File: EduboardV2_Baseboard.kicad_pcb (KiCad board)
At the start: 2 copper layers, 100 x 160 mm, 167 parts, among them IC201 PCF8563T_5,518, IC202 W25Q128JVSIQTR, IC301 XL1509-5.0E1, IC302 SY8113BADC, IC501 USB2514BI-AEZG-TR, IC601 SP3485EN-L_TR, IC602 WM8782SEDS_RV_C323842, IC603 STK8321, IC604 CS4344-CZZ, IC605 STK8321, IC606 MCP9700AT-E_TT, J501 Conn_WS2812_Extern, Q301 AO3401A, Q302 AO3400A, Q303 AO3401A, Q304 AO3401A, SW301 1FS1T1B9M2RES-5, SW401 K2-1102SP-C4SC-04, SW402 K2-1102SP-C4SC-04, SW403 K2-1102SP-C4SC-04, SW404 K2-1102SP-C4SC-04, SW405 PEC11R-4220F-S0012, T401 AO3400A, T402 AO3400A, T403 AO3400A, T404 AO3400A, T405 AO3400A, T406 AO3400A, T501 AO3400A, T502 AO3400A, X201 PCIE-52P40H, X202 32.768 kHz, X203 TF-15×15, X204 CR1220-2ZX, X301 KF2EDGR-3.81-3P, X401 ER-TFT035-6, X501 BH-00105, X502 USB3.1C16PFSMT, X503 USB3.1C16PFSMT, X504 S4B-PH-SM4-K-TB(LF)(SN), X505 PJ-327C-4A, X506 PJ-327C-4A, X507 KF2EDGR-3.81-3P, X601 CH340G, Y601 X322512MSB4SI

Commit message: start rework of baseboard.
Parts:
- removed BUZZER401: MLT-8530, eduboardv2:BUZ-SMD_4P-L8.5-W8.5-P8.50-TL
- removed C201: 10pF, eduboardv2:C0402
- removed C202, C410, C411: 1uF, eduboardv2:C0402
- removed C203, C402, C404, C406, C408: 10nF, eduboardv2:C0402
- removed C204, C407, C409, C604, C606, C608: 100nF, eduboardv2:C0402
- removed C301, C305, C312: 220uF, 35V, eduboardv2:CAP-SMD_BD8.0-L8.3-W8.3-RD
- removed C302, C307, C310, C601, C605: 100nF, 50V, eduboardv2:C0402
- removed C303, C306, C309: 10uF, X5R, 25V, eduboardv2:C0603
- removed C304, C602, C603: 22pF, eduboardv2:C0402
- removed C308, C311: 1uF, 25V, eduboardv2:C0402
- removed C401, C403, C405: 1nF, eduboardv2:C0402
- removed C607, C609: 10uF, eduboardv2:C0603
- removed C610, C611: 4.7uF, eduboardv2:C0603
- removed C612, C613: 2.2nF, eduboardv2:C0402
- removed D201, D202: B5819W_C8598, eduboardv2:SOD-123_L2.7-W1.6-LS3.7-RD-1
- removed D301, D302: SS210, eduboardv2:SMA_L4.3-W2.6-LS5.2-RD
- removed D303, D401, D402, D403, D404, D405, D406, D407, D408: blue, eduboardv2:LED0603-R-RD_BLUE
- removed D409: RGB-LED, eduboardv2:LED-SMD_FM-B2020RGBA-HG
- removed D410: WS2812B-B_W, eduboardv2:LED-SMD_4P-L5.0-W5.0-TL_WS2812B-B
- removed D411: 1N4148WST4, eduboardv2:SOD-323_L1.8-W1.3-LS2.5-RD
- removed D501, D502: PRTR5V0U2X_C2827688, eduboardv2:SOT-143-4_L2.9-W1.3-P1.92-LS2.4-BL
- removed IC201: PCF8563T_5,518, eduboardv2:SOIC-8_L5.0-W4.0-P1.27-LS6.0-BL
- removed IC202: W25Q128JVSIQTR, eduboardv2:SOIC-8_L5.3-W5.3-P1.27-LS8.0-BL
- removed IC301: XL1509-5.0E1, eduboardv2:SOIC-8_L5.0-W4.0-P1.27-LS6.0-BL
- removed IC302: SY8113BADC, eduboardv2:TSOT-23-6_L2.9-W1.6-P0.95-LS2.8-BR
- removed IC501: USB2514BI-AEZG-TR, eduboardv2:QFN-36_L6.0-W6.0-P0.50-BL-EP
- removed IC601: SP3485EN-L_TR, eduboardv2:SOIC-8_L5.0-W4.0-P1.27-LS6.0-BL
- removed IC602: WM8782SEDS_RV_C323842, eduboardv2:SSOP-20_L7.5-W5.2-P0.65-LS8.0-BL
- removed IC603, IC605: STK8321, eduboardv2:LGA-12_L2.0-W2.0-P0.50-TR
- removed IC604: CS4344-CZZ, eduboardv2:TSSOP-10_L3.0-W3.0-P0.50-LS4.9-BL
- removed IC606: MCP9700AT-E_TT, eduboardv2:SOT-23-3_L2.9-W1.3-P1.90-LS2.4-BR
- removed J501: Conn_WS2812_Extern, Connector_PinHeader_2.54mm:PinHeader_1x03_P2.54mm_Vertical
- removed JP501: Stemma Voltage Selector, Jumper:SolderJumper-3_P1.3mm_Open_RoundedPad1.0x1.5mm
- removed L301: 6.8uH, 1A, eduboardv2:IND-SMD_L4.0-W4.0
- removed L302: 68uH, 1A, eduboardv2:IND-SMD_L6.0-W6.0_FNR60XXS
- removed L601: GZ1608D601TF, eduboardv2:L0603
- removed Q301, Q303, Q304: AO3401A, eduboardv2:SOT-23_L2.9-W1.3-P1.90-LS2.4-BR
- removed Q302, T401, T402, T403, T404, T405, T406, T501, T502: AO3400A, eduboardv2:SOT-23-3_L2.9-W1.6-P1.90-LS2.8-BR
- removed R201, R202, R402, R409, R417, R421, R426, R427, R428, R429, R503, R504, R601, R603, R604, R605: 10k, eduboardv2:R0402
- removed R301, R302, R303: 1M, eduboardv2:R0402
- removed R304, R306: 100k, eduboardv2:R0402
- removed R305: 22k, eduboardv2:R0402
- removed R307, R401, R403, R405, R406, R407, R408, R410, R412, R413, R414, R416, R420: 1k, eduboardv2:R0402
- removed R404, R411, R415: 50k, eduboardv2:RES-TH_RK09K1130AAU
- removed R418, R419, R422: 150R, eduboardv2:R0402
- removed R423, R424, R425, R430, R431, R432, R434, R436, R437, R439: 10R, eduboardv2:R0402
- removed R433, R435, R438: NP, eduboardv2:R0402
- removed R501, R502: 5.1k, eduboardv2:R0402
- removed R602: 120R, eduboardv2:R0402
- removed R606, R607: 470R, eduboardv2:R0402
- removed SW301: 1FS1T1B9M2RES-5, eduboardv2:SW-TH_1FS1T1B9M2RES-5
- removed SW401, SW402, SW403, SW404: K2-1102SP-C4SC-04, eduboardv2:KEY-SMD_4P-L6.0-W6.0-P4.50-LS9.5-BL
- removed SW405: PEC11R-4220F-S0012, eduboardv2:SW-TH_PEC11R-4220F-S0012
- removed X201: PCIE-52P40H, eduboardv2:PCIE-SMD_PCIE-52P40H
- removed X202: 32.768 kHz, eduboardv2:FC-135R_L3.2-W1.5
- removed X203: TF-15×15, eduboardv2:TF-SMD_TF-15-15
- removed X204: CR1220-2ZX, eduboardv2:BAT-SMD_CR1220-2ZX
- removed X301, X507: KF2EDGR-3.81-3P, eduboardv2:CONN-TH_3P-P3.81_KF2EDGR-3.81-3P
- removed X401: ER-TFT035-6, eduboardv2:FPC-SMD_AFC07-S50ECA-00
- removed X501: BH-00105, eduboardv2:IDC-SMD_BH-00105
- removed X502, X503: USB3.1C16PFSMT, eduboardv2:USB-C-SMD_TYPE-C-USB-17
- removed X504: S4B-PH-SM4-K-TB(LF)(SN), eduboardv2:CONN-SMD_S4B-PH-SM4-K-TB-LF-SN
- removed X505, X506: PJ-327C-4A, eduboardv2:AUDIO-SMD_PJ-327C-4A
- removed X601: CH340G, eduboardv2:SOIC-16_L9.9-W3.9-P1.27-LS6.0-BL
- removed Y601: X322512MSB4SI, eduboardv2:OSC-SMD_4P-L3.2-W2.5-BL

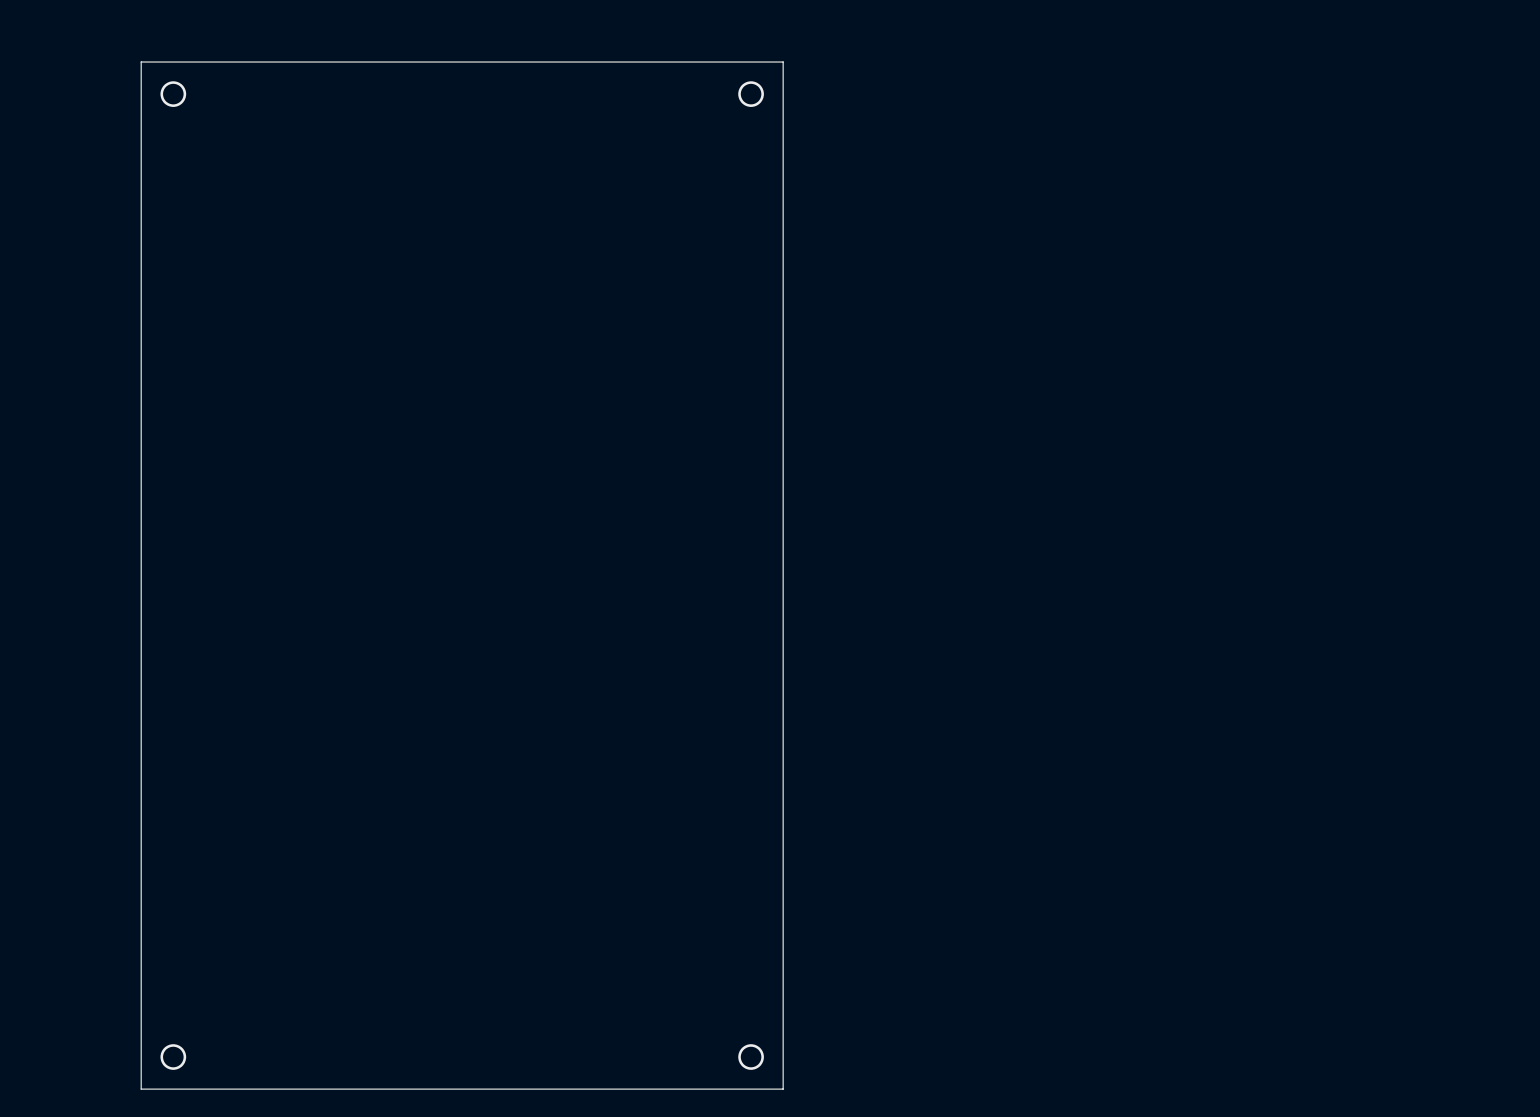
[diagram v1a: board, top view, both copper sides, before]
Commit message: replace display with better module, start layout parts on pcb.
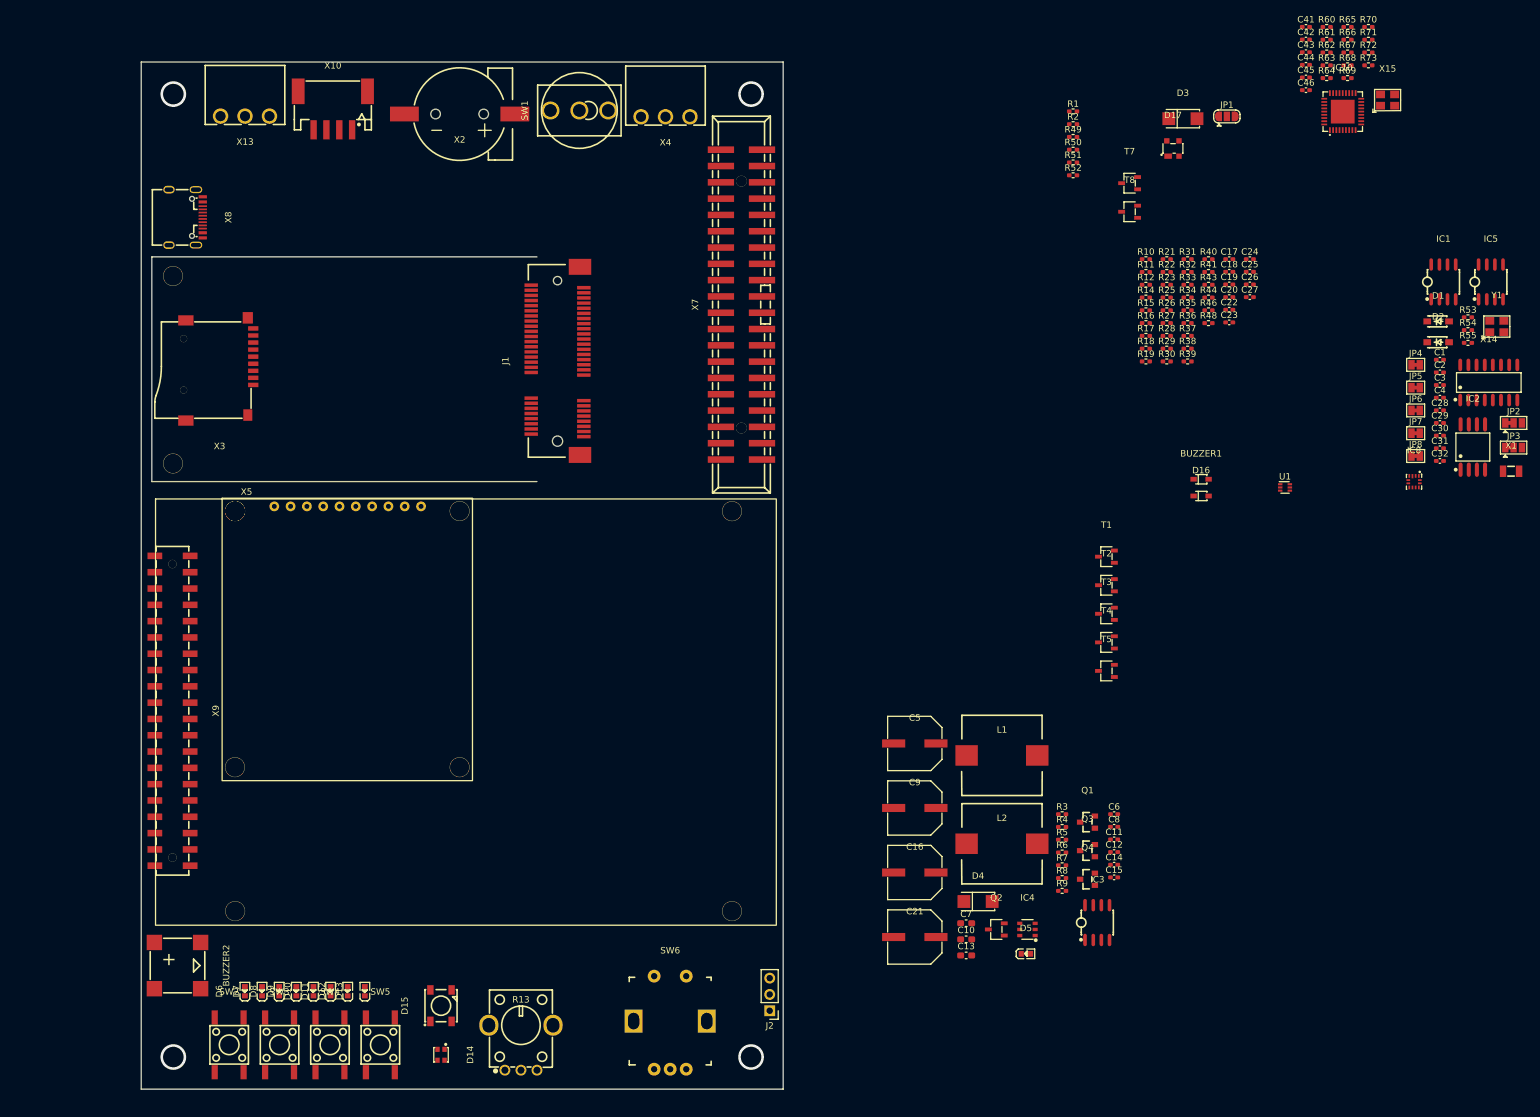
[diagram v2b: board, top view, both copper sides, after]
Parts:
- added BUZZER1: MLT-8530, EduboardV2_kicadlib:SOD-323_L1.8-W1.3-LS2.5-RD, F.Cu at (219.1, 86.0)
- added BUZZER2: MLT-8530, EduboardV2_kicadlib:BUZ-SMD_4P-L8.5-W8.5-P8.50-BR, F.Cu at (59.6, 161.8)
- added C1: 10pF, Capacitor_SMD:C_0402_1005Metric_Pad0.74x0.62mm_HandSolder, F.Cu at (256.3, 67.4)
- added C10: 10uF, X5R, 25V, Capacitor_SMD:C_0603_1608Metric_Pad1.08x0.95mm_HandSolder, F.Cu at (182.5, 157.7)
- added C11: 100nF, 50V, Capacitor_SMD:C_0402_1005Metric_Pad0.74x0.62mm_HandSolder, F.Cu at (205.6, 142.1)
- added C12: 1uF, 25V, Capacitor_SMD:C_0402_1005Metric_Pad0.74x0.62mm_HandSolder, F.Cu at (205.6, 144.1)
- added C13: 10uF, X5R, 25V, Capacitor_SMD:C_0603_1608Metric_Pad1.08x0.95mm_HandSolder, F.Cu at (182.5, 160.2)
- added C14: 100nF, 50V, Capacitor_SMD:C_0402_1005Metric_Pad0.74x0.62mm_HandSolder, F.Cu at (205.6, 146.0)
- added C15: 1uF, 25V, Capacitor_SMD:C_0402_1005Metric_Pad0.74x0.62mm_HandSolder, F.Cu at (205.6, 148.0)
- added C16: 220uF, 35V, EduboardV2_kicadlib:CAP-SMD_BD8.0-L8.3-W8.3-RD, F.Cu at (174.5, 147.3)
- added C17: 1nF, Capacitor_SMD:C_0402_1005Metric_Pad0.74x0.62mm_HandSolder, F.Cu at (223.5, 51.7)
- added C18: 10nF, Capacitor_SMD:C_0402_1005Metric_Pad0.74x0.62mm_HandSolder, F.Cu at (223.5, 53.7)
- added C19: 100nF, Capacitor_SMD:C_0402_1005Metric_Pad0.74x0.62mm_HandSolder, F.Cu at (223.5, 55.7)
- added C2: 1uF, Capacitor_SMD:C_0402_1005Metric_Pad0.74x0.62mm_HandSolder, F.Cu at (256.3, 69.4)
- added C20: 10nF, Capacitor_SMD:C_0402_1005Metric_Pad0.74x0.62mm_HandSolder, F.Cu at (223.5, 57.6)
- added C21: 220uF, 35V, EduboardV2_kicadlib:CAP-SMD_BD8.0-L8.3-W8.3-RD, F.Cu at (174.5, 157.3)
- added C22: 10nF, Capacitor_SMD:C_0402_1005Metric_Pad0.74x0.62mm_HandSolder, F.Cu at (223.5, 59.6)
- added C23: 100nF, Capacitor_SMD:C_0402_1005Metric_Pad0.74x0.62mm_HandSolder, F.Cu at (223.5, 61.6)
- added C24: 10nF, Capacitor_SMD:C_0402_1005Metric_Pad0.74x0.62mm_HandSolder, F.Cu at (226.7, 51.7)
- added C25: 100nF, Capacitor_SMD:C_0402_1005Metric_Pad0.74x0.62mm_HandSolder, F.Cu at (226.7, 53.7)
- added C26: 1uF, Capacitor_SMD:C_0402_1005Metric_Pad0.74x0.62mm_HandSolder, F.Cu at (226.7, 55.7)
- added C27: 1uF, Capacitor_SMD:C_0402_1005Metric_Pad0.74x0.62mm_HandSolder, F.Cu at (226.7, 57.6)
- added C28: 100nF, 50V, Capacitor_SMD:C_0402_1005Metric_Pad0.74x0.62mm_HandSolder, F.Cu at (256.3, 75.3)
- added C29: 22pF, Capacitor_SMD:C_0402_1005Metric_Pad0.74x0.62mm_HandSolder, F.Cu at (256.3, 77.2)
- added C3: 10nF, Capacitor_SMD:C_0402_1005Metric_Pad0.74x0.62mm_HandSolder, F.Cu at (256.3, 71.3)
- added C30: 22pF, Capacitor_SMD:C_0402_1005Metric_Pad0.74x0.62mm_HandSolder, F.Cu at (256.3, 79.2)
- added C31: 100nF, Capacitor_SMD:C_0402_1005Metric_Pad0.74x0.62mm_HandSolder, F.Cu at (256.3, 81.2)
- added C32: 100nF, 50V, Capacitor_SMD:C_0402_1005Metric_Pad0.74x0.62mm_HandSolder, F.Cu at (256.3, 83.1)
- added C4: 100nF, Capacitor_SMD:C_0402_1005Metric_Pad0.74x0.62mm_HandSolder, F.Cu at (256.3, 73.3)
- added C41: 100nF, 50V, Capacitor_SMD:C_0402_1005Metric_Pad0.74x0.62mm_HandSolder, F.Cu at (235.4, 15.5)
- added C42: CL05C100JB5NNNC, Capacitor_SMD:C_0402_1005Metric_Pad0.74x0.62mm_HandSolder, F.Cu at (235.4, 17.5)
- added C43: 100nF, 50V, Capacitor_SMD:C_0402_1005Metric_Pad0.74x0.62mm_HandSolder, F.Cu at (235.4, 19.5)
- added C44: CL05C100JB5NNNC, Capacitor_SMD:C_0402_1005Metric_Pad0.74x0.62mm_HandSolder, F.Cu at (235.4, 21.4)
- added C45: 100nF, 50V, Capacitor_SMD:C_0402_1005Metric_Pad0.74x0.62mm_HandSolder, F.Cu at (235.4, 23.4)
- added C46: 100nF, 50V, Capacitor_SMD:C_0402_1005Metric_Pad0.74x0.62mm_HandSolder, F.Cu at (235.4, 25.4)
- added C5: 220uF, 35V, EduboardV2_kicadlib:CAP-SMD_BD8.0-L8.3-W8.3-RD, F.Cu at (174.5, 127.2)
- added C6: 100nF, 50V, Capacitor_SMD:C_0402_1005Metric_Pad0.74x0.62mm_HandSolder, F.Cu at (205.6, 138.2)
- added C7: 10uF, X5R, 25V, Capacitor_SMD:C_0603_1608Metric_Pad1.08x0.95mm_HandSolder, F.Cu at (182.5, 155.2)
- added C8: 22pF, Capacitor_SMD:C_0402_1005Metric_Pad0.74x0.62mm_HandSolder, F.Cu at (205.6, 140.1)
- added C9: 220uF, 35V, EduboardV2_kicadlib:CAP-SMD_BD8.0-L8.3-W8.3-RD, F.Cu at (174.5, 137.2)
- added D1: B5819W_C8598, EduboardV2_kicadlib:SOD-123_L2.7-W1.6-LS3.7-RD-1, F.Cu at (256.0, 61.4)
- added D10: blue, EduboardV2_kicadlib:LED0603-FD_BLUE, F.Cu at (80.8, 165.8)
- added D11: blue, EduboardV2_kicadlib:LED0603-FD_BLUE, F.Cu at (83.5, 165.8)
- added D12: blue, EduboardV2_kicadlib:LED0603-FD_BLUE, F.Cu at (86.2, 165.8)
- added D13: blue, EduboardV2_kicadlib:LED0603-FD_BLUE, F.Cu at (88.8, 165.8)
- added D14: RGB-LED, EduboardV2_kicadlib:LED-SMD_FM-B2020RGBA-HG, F.Cu at (100.7, 175.7)
- added D15: WS2812B-B_W, EduboardV2_kicadlib:LED-SMD_4P-L5.0-W5.0-TL_WS2812B-B, F.Cu at (100.7, 168.0)
- added D16: 1N4148WST4, EduboardV2_kicadlib:SOD-323_L1.8-W1.3-LS2.5-RD, F.Cu at (219.1, 88.6)
- added D17: PRTR5V0U2X_C2827688, EduboardV2_kicadlib:SOT-143-4_L2.9-W1.3-P1.92-LS2.4-BL, F.Cu at (214.7, 34.5)
- added D2: B5819W_C8598, EduboardV2_kicadlib:SOD-123_L2.7-W1.6-LS3.7-RD-1, F.Cu at (256.0, 64.7)
- added D3: SS210, EduboardV2_kicadlib:SMA_L4.3-W2.6-LS5.2-RD, F.Cu at (216.3, 29.8)
- added D4: SS210, EduboardV2_kicadlib:SMA_L4.3-W2.6-LS5.2-RD, F.Cu at (184.4, 151.8)
- added D5: blue, EduboardV2_kicadlib:LED0603-FD_BLUE, F.Cu at (191.8, 159.9)
- added D6: blue, EduboardV2_kicadlib:LED0603-FD_BLUE, F.Cu at (70.2, 165.8)
- added D7: blue, EduboardV2_kicadlib:LED0603-FD_BLUE, F.Cu at (72.8, 165.8)
- added D8: blue, EduboardV2_kicadlib:LED0603-FD_BLUE, F.Cu at (75.5, 165.8)
- added D9: blue, EduboardV2_kicadlib:LED0603-FD_BLUE, F.Cu at (78.2, 165.8)
- added IC1: PCF8563T_5,518, EduboardV2_kicadlib:SOIC-8_L5.0-W4.0-P1.27-LS6.0-BL, F.Cu at (256.9, 55.3)
- added IC10: USB2514BI-AEZG-TR, EduboardV2_kicadlib:TQFN-36_L6.0-W6.0-P0.50-BL-EP3.7, F.Cu at (241.2, 28.7)
- added IC2: W25Q128JVSIQTR, EduboardV2_kicadlib:SOIC-8_L5.3-W5.3-P1.27-LS8.0-BL, F.Cu at (261.4, 81.0)
- added IC3: XL1509-5.0E1, EduboardV2_kicadlib:SOIC-8_L5.0-W4.0-P1.27-LS6.0-BL, F.Cu at (202.9, 155.1)
- added IC4: SY8113BADC, EduboardV2_kicadlib:TSOT-23-6_L2.9-W1.6-P0.95-LS2.8-BR, F.Cu at (192.1, 156.1)
- added IC5: SP3485EN-L_TR, EduboardV2_kicadlib:SOIC-8_L5.0-W4.0-P1.27-LS6.0-BL, F.Cu at (264.2, 55.3)
- added IC8: STK8321, EduboardV2_kicadlib:LGA-12_L2.0-W2.0-P0.50-TR, F.Cu at (252.3, 86.4)
- added J1: EduboardV2 PCIE UP Board Connector, EduboardV2_kicadlib:CONN-SMD_52P-P0.80-V_91304-70-052RXXX, F.Cu at (118.8, 67.6)
- added J2: Conn_WS2812_Extern, Connector_PinHeader_2.54mm:PinHeader_1x03_P2.54mm_Vertical, F.Cu at (151.9, 168.8)
- added JP1: Stemma Voltage Selector, Jumper:SolderJumper-3_P1.3mm_Open_RoundedPad1.0x1.5mm, F.Cu at (223.1, 29.5)
- added JP2: SolderJumper_3_Bridged12, Jumper:SolderJumper-3_P1.3mm_Bridged12_Pad1.0x1.5mm, F.Cu at (267.8, 77.2)
- added JP3: SolderJumper_3_Bridged12, Jumper:SolderJumper-3_P1.3mm_Bridged12_Pad1.0x1.5mm, F.Cu at (267.8, 81.1)
- added JP4: SolderJumper_2_Bridged, Jumper:SolderJumper-2_P1.3mm_Bridged_Pad1.0x1.5mm, F.Cu at (252.5, 68.2)
- added JP5: SolderJumper_2_Bridged, Jumper:SolderJumper-2_P1.3mm_Bridged_Pad1.0x1.5mm, F.Cu at (252.5, 71.7)
- added JP6: SolderJumper_2_Bridged, Jumper:SolderJumper-2_P1.3mm_Bridged_Pad1.0x1.5mm, F.Cu at (252.5, 75.3)
- added JP7: SolderJumper_2_Bridged, Jumper:SolderJumper-2_P1.3mm_Bridged_Pad1.0x1.5mm, F.Cu at (252.5, 78.8)
- added JP8: SolderJumper_2_Bridged, Jumper:SolderJumper-2_P1.3mm_Bridged_Pad1.0x1.5mm, F.Cu at (252.5, 82.4)
- added L1: SLF12565T-680M2R0-PF, EduboardV2_kicadlib:IND-SMD_L12.5-W12.5_SLF12565T, F.Cu at (188.1, 129.0)
- added L2: SLF12565T-680M2R0-PF, EduboardV2_kicadlib:IND-SMD_L12.5-W12.5_SLF12565T, F.Cu at (188.1, 142.8)
- added Q1: AO3401A, EduboardV2_kicadlib:SOT-23_L2.9-W1.3-P1.90-LS2.4-BR, F.Cu at (201.4, 139.4)
- added Q2: AO3400A, EduboardV2_kicadlib:SOT-23-3_L2.9-W1.6-P1.90-LS2.8-BR, F.Cu at (187.2, 156.1)
- added Q3: AO3401A, EduboardV2_kicadlib:SOT-23_L2.9-W1.3-P1.90-LS2.4-BR, F.Cu at (201.4, 143.9)
- added Q4: AO3401A, EduboardV2_kicadlib:SOT-23_L2.9-W1.3-P1.90-LS2.4-BR, F.Cu at (201.4, 148.3)
- added R1: 10k, Resistor_SMD:R_0402_1005Metric_Pad0.72x0.64mm_HandSolder, F.Cu at (199.2, 28.7)
- added R10: 1k, Resistor_SMD:R_0402_1005Metric_Pad0.72x0.64mm_HandSolder, F.Cu at (210.5, 51.7)
- added R11: 10k, Resistor_SMD:R_0402_1005Metric_Pad0.72x0.64mm_HandSolder, F.Cu at (210.5, 53.7)
- added R12: 1k, Resistor_SMD:R_0402_1005Metric_Pad0.72x0.64mm_HandSolder, F.Cu at (210.5, 55.7)
- added R13: 50k, EduboardV2_kicadlib:RES-TH_RK09K1130AAU, F.Cu at (113.2, 174.6)
- added R14: 1k, Resistor_SMD:R_0402_1005Metric_Pad0.72x0.64mm_HandSolder, F.Cu at (210.5, 57.7)
- added R15: 1k, Resistor_SMD:R_0402_1005Metric_Pad0.72x0.64mm_HandSolder, F.Cu at (210.5, 59.7)
- added R16: 1k, Resistor_SMD:R_0402_1005Metric_Pad0.72x0.64mm_HandSolder, F.Cu at (210.5, 61.7)
- added R17: 1k, Resistor_SMD:R_0402_1005Metric_Pad0.72x0.64mm_HandSolder, F.Cu at (210.5, 63.7)
- added R18: 10k, Resistor_SMD:R_0402_1005Metric_Pad0.72x0.64mm_HandSolder, F.Cu at (210.5, 65.7)
- added R19: 1k, Resistor_SMD:R_0402_1005Metric_Pad0.72x0.64mm_HandSolder, F.Cu at (210.5, 67.6)
- added R2: 10k, Resistor_SMD:R_0402_1005Metric_Pad0.72x0.64mm_HandSolder, F.Cu at (199.2, 30.7)
- added R21: 1k, Resistor_SMD:R_0402_1005Metric_Pad0.72x0.64mm_HandSolder, F.Cu at (213.8, 51.7)
- added R22: 1k, Resistor_SMD:R_0402_1005Metric_Pad0.72x0.64mm_HandSolder, F.Cu at (213.8, 53.7)
- added R23: 1k, Resistor_SMD:R_0402_1005Metric_Pad0.72x0.64mm_HandSolder, F.Cu at (213.8, 55.7)
- added R25: 1k, Resistor_SMD:R_0402_1005Metric_Pad0.72x0.64mm_HandSolder, F.Cu at (213.8, 57.7)
- added R26: 10k, Resistor_SMD:R_0402_1005Metric_Pad0.72x0.64mm_HandSolder, F.Cu at (213.8, 59.7)
- added R27: 150R, Resistor_SMD:R_0402_1005Metric_Pad0.72x0.64mm_HandSolder, F.Cu at (213.8, 61.7)
- added R28: 150R, Resistor_SMD:R_0402_1005Metric_Pad0.72x0.64mm_HandSolder, F.Cu at (213.8, 63.7)
- added R29: 1k, Resistor_SMD:R_0402_1005Metric_Pad0.72x0.64mm_HandSolder, F.Cu at (213.8, 65.7)
- added R3: 1M, Resistor_SMD:R_0402_1005Metric_Pad0.72x0.64mm_HandSolder, F.Cu at (197.5, 138.2)
- added R30: 10k, Resistor_SMD:R_0402_1005Metric_Pad0.72x0.64mm_HandSolder, F.Cu at (213.8, 67.6)
- added R31: 150R, Resistor_SMD:R_0402_1005Metric_Pad0.72x0.64mm_HandSolder, F.Cu at (217.0, 51.7)
- added R32: 10R, Resistor_SMD:R_0402_1005Metric_Pad0.72x0.64mm_HandSolder, F.Cu at (217.0, 53.7)
- added R33: 10R, Resistor_SMD:R_0402_1005Metric_Pad0.72x0.64mm_HandSolder, F.Cu at (217.0, 55.7)
- added R34: 10R, Resistor_SMD:R_0402_1005Metric_Pad0.72x0.64mm_HandSolder, F.Cu at (217.0, 57.7)
- added R35: 10k, Resistor_SMD:R_0402_1005Metric_Pad0.72x0.64mm_HandSolder, F.Cu at (217.0, 59.7)
- added R36: 10k, Resistor_SMD:R_0402_1005Metric_Pad0.72x0.64mm_HandSolder, F.Cu at (217.0, 61.7)
- added R37: 10k, Resistor_SMD:R_0402_1005Metric_Pad0.72x0.64mm_HandSolder, F.Cu at (217.0, 63.7)
- added R38: 10k, Resistor_SMD:R_0402_1005Metric_Pad0.72x0.64mm_HandSolder, F.Cu at (217.0, 65.7)
- added R39: 10R, Resistor_SMD:R_0402_1005Metric_Pad0.72x0.64mm_HandSolder, F.Cu at (217.0, 67.6)
- added R4: 1M, Resistor_SMD:R_0402_1005Metric_Pad0.72x0.64mm_HandSolder, F.Cu at (197.5, 140.2)
- added R40: 10R, Resistor_SMD:R_0402_1005Metric_Pad0.72x0.64mm_HandSolder, F.Cu at (220.3, 51.7)
- added R41: 10R, Resistor_SMD:R_0402_1005Metric_Pad0.72x0.64mm_HandSolder, F.Cu at (220.3, 53.7)
- added R43: 10R, Resistor_SMD:R_0402_1005Metric_Pad0.72x0.64mm_HandSolder, F.Cu at (220.3, 55.7)
- added R44: NP, Resistor_SMD:R_0402_1005Metric_Pad0.72x0.64mm_HandSolder, F.Cu at (220.3, 57.7)
- added R46: 10R, Resistor_SMD:R_0402_1005Metric_Pad0.72x0.64mm_HandSolder, F.Cu at (220.3, 59.7)
- added R48: 10R, Resistor_SMD:R_0402_1005Metric_Pad0.72x0.64mm_HandSolder, F.Cu at (220.3, 61.7)
- added R49: 5.1k, Resistor_SMD:R_0402_1005Metric_Pad0.72x0.64mm_HandSolder, F.Cu at (199.2, 32.7)
- added R5: 1M, Resistor_SMD:R_0402_1005Metric_Pad0.72x0.64mm_HandSolder, F.Cu at (197.5, 142.2)
- added R50: 5.1k, Resistor_SMD:R_0402_1005Metric_Pad0.72x0.64mm_HandSolder, F.Cu at (199.2, 34.7)
- added R51: 10k, Resistor_SMD:R_0402_1005Metric_Pad0.72x0.64mm_HandSolder, F.Cu at (199.2, 36.7)
- added R52: 10k, Resistor_SMD:R_0402_1005Metric_Pad0.72x0.64mm_HandSolder, F.Cu at (199.2, 38.6)
- added R53: 10k, Resistor_SMD:R_0402_1005Metric_Pad0.72x0.64mm_HandSolder, F.Cu at (260.7, 60.8)
- added R54: 120R, Resistor_SMD:R_0402_1005Metric_Pad0.72x0.64mm_HandSolder, F.Cu at (260.7, 62.8)
- added R55: 10k, Resistor_SMD:R_0402_1005Metric_Pad0.72x0.64mm_HandSolder, F.Cu at (260.7, 64.8)
- added R6: 100k, Resistor_SMD:R_0402_1005Metric_Pad0.72x0.64mm_HandSolder, F.Cu at (197.5, 144.1)
- added R60: 10k, Resistor_SMD:R_0402_1005Metric_Pad0.72x0.64mm_HandSolder, F.Cu at (238.7, 15.5)
- added R61: 10k, Resistor_SMD:R_0402_1005Metric_Pad0.72x0.64mm_HandSolder, F.Cu at (238.7, 17.5)
- added R62: 10k, Resistor_SMD:R_0402_1005Metric_Pad0.72x0.64mm_HandSolder, F.Cu at (238.7, 19.5)
- added R63: 10k, Resistor_SMD:R_0402_1005Metric_Pad0.72x0.64mm_HandSolder, F.Cu at (238.7, 21.5)
- added R64: 1M, Resistor_SMD:R_0402_1005Metric_Pad0.72x0.64mm_HandSolder, F.Cu at (238.7, 23.5)
- added R65: 12k, Resistor_SMD:R_0402_1005Metric_Pad0.72x0.64mm_HandSolder, F.Cu at (241.9, 15.5)
- added R66: 47k, Resistor_SMD:R_0402_1005Metric_Pad0.72x0.64mm_HandSolder, F.Cu at (241.9, 17.5)
- added R67: 47k, Resistor_SMD:R_0402_1005Metric_Pad0.72x0.64mm_HandSolder, F.Cu at (241.9, 19.5)
- added R68: 47k, Resistor_SMD:R_0402_1005Metric_Pad0.72x0.64mm_HandSolder, F.Cu at (241.9, 21.5)
- added R69: 47k, Resistor_SMD:R_0402_1005Metric_Pad0.72x0.64mm_HandSolder, F.Cu at (241.9, 23.5)
- added R7: 22k, Resistor_SMD:R_0402_1005Metric_Pad0.72x0.64mm_HandSolder, F.Cu at (197.5, 146.1)
- added R70: 100k, Resistor_SMD:R_0402_1005Metric_Pad0.72x0.64mm_HandSolder, F.Cu at (245.2, 15.5)
- added R71: 100k, Resistor_SMD:R_0402_1005Metric_Pad0.72x0.64mm_HandSolder, F.Cu at (245.2, 17.5)
- added R72: 100k, Resistor_SMD:R_0402_1005Metric_Pad0.72x0.64mm_HandSolder, F.Cu at (245.2, 19.5)
- added R73: 12k, Resistor_SMD:R_0402_1005Metric_Pad0.72x0.64mm_HandSolder, F.Cu at (245.2, 21.5)
- added R8: 100k, Resistor_SMD:R_0402_1005Metric_Pad0.72x0.64mm_HandSolder, F.Cu at (197.5, 148.1)
- added R9: 1k, Resistor_SMD:R_0402_1005Metric_Pad0.72x0.64mm_HandSolder, F.Cu at (197.5, 150.1)
- added SW1: 1FS1T1B9M2RES-5, EduboardV2_kicadlib:SW-TH_1FS1T1B9M2RES-5, F.Cu at (122.2, 28.6)
- added SW2: K2-1102SP-C4SC-04, EduboardV2_kicadlib:KEY-SMD_4P-L6.0-W6.0-P4.50-LS9.5-BL, F.Cu at (67.7, 174.1)
- added SW3: K2-1102SP-C4SC-04, EduboardV2_kicadlib:KEY-SMD_4P-L6.0-W6.0-P4.50-LS9.5-BL, F.Cu at (75.5, 174.1)
- added SW4: K2-1102SP-C4SC-04, EduboardV2_kicadlib:KEY-SMD_4P-L6.0-W6.0-P4.50-LS9.5-BL, F.Cu at (83.4, 174.1)
- added SW5: K2-1102SP-C4SC-04, EduboardV2_kicadlib:KEY-SMD_4P-L6.0-W6.0-P4.50-LS9.5-BL, F.Cu at (91.2, 174.1)
- added SW6: PEC11R-4220F-S0012, EduboardV2_kicadlib:SW-TH_PEC11R-4220F-S0012, F.Cu at (136.4, 170.7)
- added T1: AO3400A, EduboardV2_kicadlib:SOT-23-3_L2.9-W1.6-P1.90-LS2.8-BR, F.Cu at (204.4, 98.1)
- added T2: AO3400A, EduboardV2_kicadlib:SOT-23-3_L2.9-W1.6-P1.90-LS2.8-BR, F.Cu at (204.4, 102.5)
- added T3: AO3400A, EduboardV2_kicadlib:SOT-23-3_L2.9-W1.6-P1.90-LS2.8-BR, F.Cu at (204.4, 107.0)
- added T4: AO3400A, EduboardV2_kicadlib:SOT-23-3_L2.9-W1.6-P1.90-LS2.8-BR, F.Cu at (204.4, 111.4)
- added T5: AO3400A, EduboardV2_kicadlib:SOT-23-3_L2.9-W1.6-P1.90-LS2.8-BR, F.Cu at (204.4, 115.9)
- added T7: AO3400A, EduboardV2_kicadlib:SOT-23-3_L2.9-W1.6-P1.90-LS2.8-BR, F.Cu at (208.0, 39.9)
- added T8: AO3400A, EduboardV2_kicadlib:SOT-23-3_L2.9-W1.6-P1.90-LS2.8-BR, F.Cu at (208.0, 44.3)
- added U1: TMP112xxDRL, Package_TO_SOT_SMD:SOT-563, F.Cu at (232.2, 87.3)
- added X1: 32.768 kHz, EduboardV2_kicadlib:FC-135R_L3.2-W1.5, F.Cu at (267.4, 84.7)
- added X10: S4B-PH-SM4-K-TB(LF)(SN), EduboardV2_kicadlib:CONN-SMD_S4B-PH-SM4-K-TB-LF-SN, F.Cu at (83.8, 28.6)
- added X13: KF2EDGR-3.81-3P, EduboardV2_kicadlib:CONN-TH_3P-P3.81_KF2EDGR-3.81-3P, F.Cu at (70.2, 29.4)
- added X14: CH340G, EduboardV2_kicadlib:SOIC-16_L9.9-W3.9-P1.27-LS6.0-BL, F.Cu at (263.9, 70.9)
- added X15: DSX321G 24MHz, EduboardV2_kicadlib:OSC-SMD_4P-L3.2-W2.5-BL, F.Cu at (248.2, 26.9)
- added X2: CR1220-2ZX, EduboardV2_kicadlib:BAT-SMD_CR1220-2ZX, F.Cu at (103.6, 29.1)
- added X3: TF-15×15, EduboardV2_kicadlib:TF-SMD_TF-15-15, F.Cu at (66.2, 68.8)
- added X4: KF2EDGR-3.81-3P, EduboardV2_kicadlib:CONN-TH_3P-P3.81_KF2EDGR-3.81-3P, F.Cu at (135.7, 29.5)
- added X5: DFR0649, EduboardV2_kicadlib:DFR0649, F.Cu at (86.3, 108.5)
- added X7: BH-00105, EduboardV2_kicadlib:IDC-SMD_BH-00105, F.Cu at (147.5, 58.8)
- added X8: USB3.1C16PFSMT, EduboardV2_kicadlib:USB-C-SMD_TYPE-C-USB-17, F.Cu at (61.0, 45.2)
- added X9: ~, EduboardV2_kicadlib:HDR-SMD_40P-P2.54-V-F-R2-C20-S7.1-EH, F.Cu at (59.0, 122.1)
- added Y1: X322512MSB4SI, EduboardV2_kicadlib:OSC-SMD_4P-L3.2-W2.5-BL, F.Cu at (265.2, 62.2)

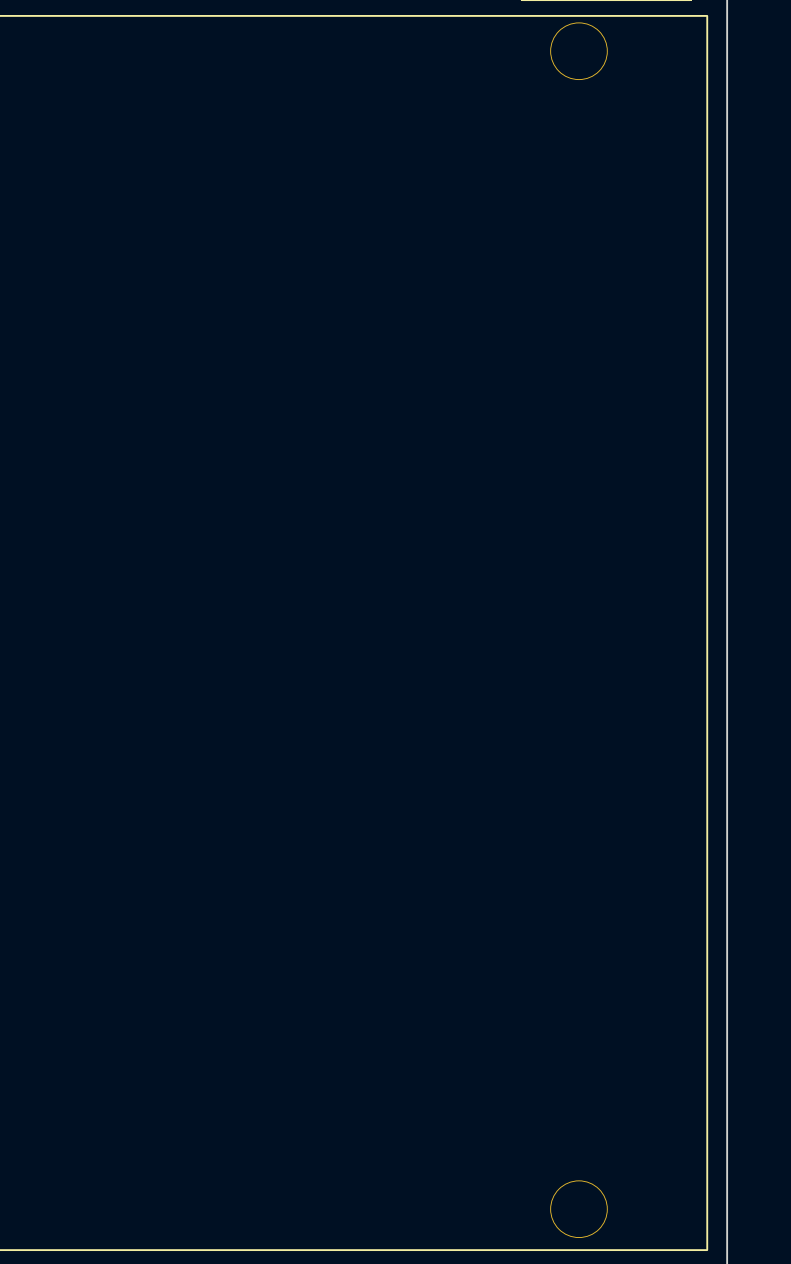
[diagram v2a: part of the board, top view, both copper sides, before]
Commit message: add protoboard area. not yet done
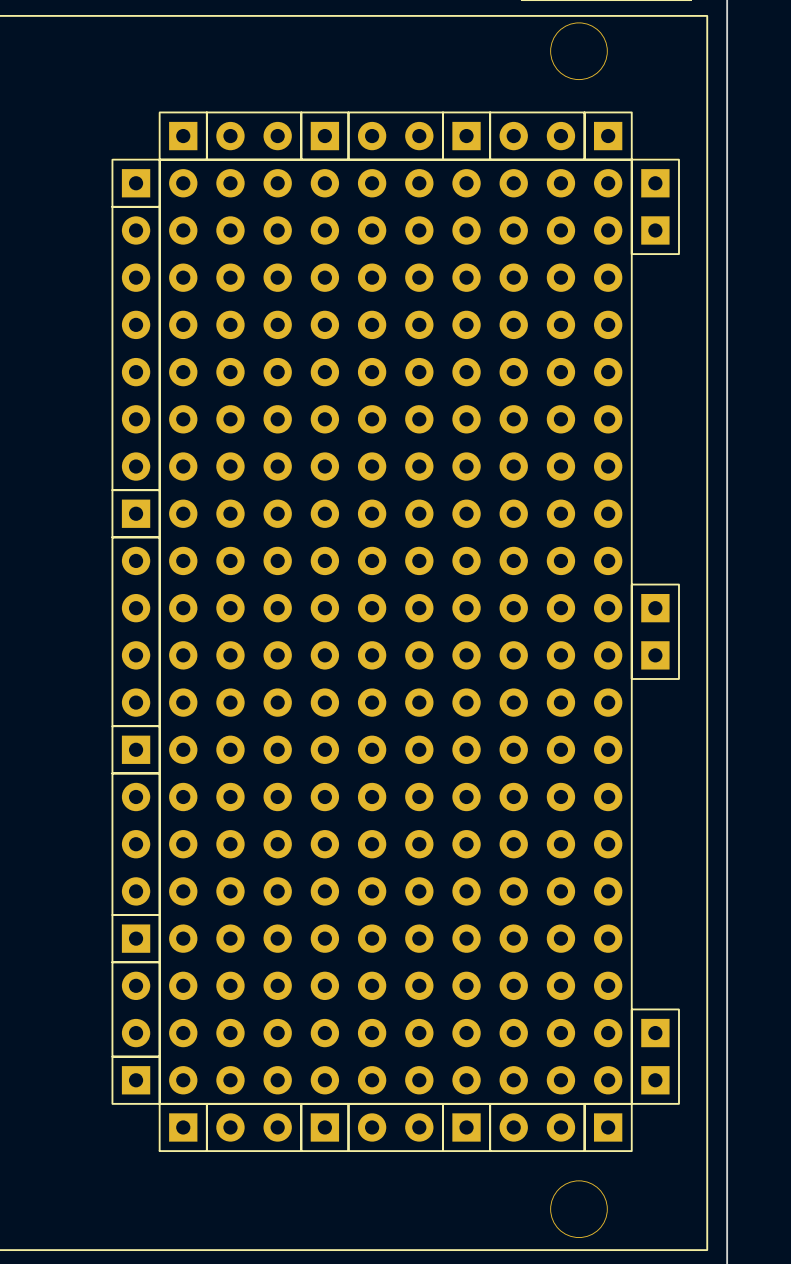
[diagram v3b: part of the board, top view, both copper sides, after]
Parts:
- added X6: ~, EduboardV2_kicadlib:protoboard_patch, F.Cu at (122.2, 148.9)
